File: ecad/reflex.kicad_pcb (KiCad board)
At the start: 2 copper layers, 20 x 60 mm, 29 parts, among them J1 USB_MICRO_B_SMD_2, J2 CONN_02X04_RA, Q1 BPW85C, SW1 CHERRY_MX1A-E1NW_BLUE, SW2 B3U-3000P_SPST-NO_SMD, U1 USBLC6, U2 ATSAMD21E18A, U3 AP2112K-3.3, U4 APA102-2020, X1 SWD_SMT_SOCKET

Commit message: Continued placement concepts and packaging ideas
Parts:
- removed D4: LED_YELLOW_1608M, Applidyne_LED:LEDC1608X80L40N
- removed D5: LED_GREEN_1608M, Applidyne_LED:LEDC1608X80L40N
- removed D7: BAV99, Applidyne_SOT:SOT95P240X110-3L16N
- removed R5, R6: 1K50_1608M, Applidyne_Resistor:RESC1608X50N
- added D3: BAV99_DUAL, Applidyne_SOT:SOT-363-6N, F.Cu at (99.5, 105.5)
- added U5: APA102-2020, Applidyne_LED:AP102_200X200X90L, F.Cu at (93.5, 116.5)
- moved C3 17.4 mm to (86.4, 93.7), turned to 270 degrees
- moved R4 15.1 mm to (82.1, 97.1)
- moved U4 14.2 mm to (93.5, 98.8), turned to 270 degrees
- moved R9 13.1 mm to (100.0, 118.5), turned to 180 degrees
- moved C2 12.7 mm to (107.2, 99.3), turned to 270 degrees
- moved R7 11.6 mm to (102.4, 104.9), turned to 270 degrees
- moved D1 3.22 mm to (96.5, 105.5)
- moved D2 3.22 mm to (93.5, 105.5)
- moved Q1 2.80 mm to (100.0, 77.8)
- moved R8 2.58 mm to (94.1, 110.2), turned to 90 degrees
- moved C1 2.40 mm to (105.0, 77.2)
- moved R2 2.40 mm to (105.1, 78.9)
- moved SW1 2.40 mm to (102.5, 82.3)
- moved U2 1.88 mm to (101.4, 98.2), turned to 0 degrees
- moved J2 0.75 mm to (97.5, 109.0)
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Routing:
- net Net-(U4-Pad1): track 0.00 -> 18.2 mm
- net Net-(U4-Pad6): track 0.00 -> 17.9 mm
- net EXTERNAL_TRIG: track 3.55 -> 17.3 mm
- net Net-(J2-Pad5): track 11.4 -> 2.18 mm
- net STATUS_CAPTURE: track 14.4 -> 6.23 mm
- net Net-(R4-Pad1): track 5.53 -> 0.00 mm
- net STATUS_USER: track 5.47 -> 0.00 mm
- net STATUS_TRIGGER: track 12.6 -> 7.37 mm
- net Net-(D5-PadA): track 4.10 -> 0.00 mm
- net Net-(J2-Pad4): track 4.27 -> 7.66 mm
- net Net-(D4-PadA): track 2.75 -> 0.00 mm
- net Net-(J2-Pad3): track 3.04 -> 5.74 mm
- net GND: track 8.90 -> 6.36 mm, vias 7 -> 4
- net UART_RX: track 8.65 -> 6.34 mm
- net UART_TX: track 8.03 -> 6.21 mm
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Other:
- board size 20 x 60 mm -> 20 x 58 mm

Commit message: Routing completed
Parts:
- F1: value 0.5A_1210L_PTC -> F1
- moved R4 25.4 mm to (107.5, 96.4), turned to 270 degrees
- moved C3 8.88 mm to (95.0, 95.9), turned to 0 degrees
- moved X1 7.47 mm to (101.7, 99.7), turned to 180 degrees
- moved R7 0.80 mm to (103.2, 104.7), turned to 0 degrees
- moved C2 0.50 mm to (107.5, 99.7)
- moved F1 0.20 mm to (99.2, 127.0)
- moved U4 0.20 mm to (93.5, 99.0)
- turned D2 to 270 degrees
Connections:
- D2 pad 3: STATUS_TRIGGER -> STATUS_CAPTURE
- D2 pad 6: STATUS_CAPTURE -> STATUS_TRIGGER
- SW2 pad 1: ~RESET -> GND
- SW2 pad 2: GND -> ~RESET
- X1 pad 7: Net-(X1-Pad7) -> PHOTO_TRANS
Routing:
- net Net-(Q1-PadC): track 0.00 -> 52.8 mm
- net +3.3V: track 6.33 -> 53.1 mm, vias 2 -> 8
- net USB_D-: track 0.00 -> 43.7 mm
- net USB_D+: track 0.00 -> 41.5 mm
- net PHOTO_TRANS: track 0.00 -> 31.2 mm, vias 0 -> 4
- net GND: track 6.36 -> 31.2 mm, vias 4 -> 14
- net ~RESET: track 0.00 -> 24.2 mm, vias 0 -> 2
- net STATUS_CAPTURE: track 6.23 -> 22.7 mm, vias 0 -> 1
- net LED_CLK: track 0.00 -> 16.1 mm, vias 0 -> 2
- net STATUS_TRIGGER: track 7.37 -> 21.9 mm, vias 0 -> 1
- net +5V: track 11.5 -> 23.8 mm
- net SWITCH_TRIG: track 11.8 -> 22.9 mm
- net LED_DATA: track 0.00 -> 10.7 mm, vias 0 -> 2
- net Net-(R4-Pad1): track 0.00 -> 10.1 mm
- net EXTERNAL_TRIG: track 17.3 -> 27.4 mm, vias 0 -> 2
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- added copper zone on B.Cu, net +3.3V
- added copper zone on B.Cu, net GND
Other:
- board size 20 x 58 mm -> 20 x 55 mm
- board text added: "1.0"

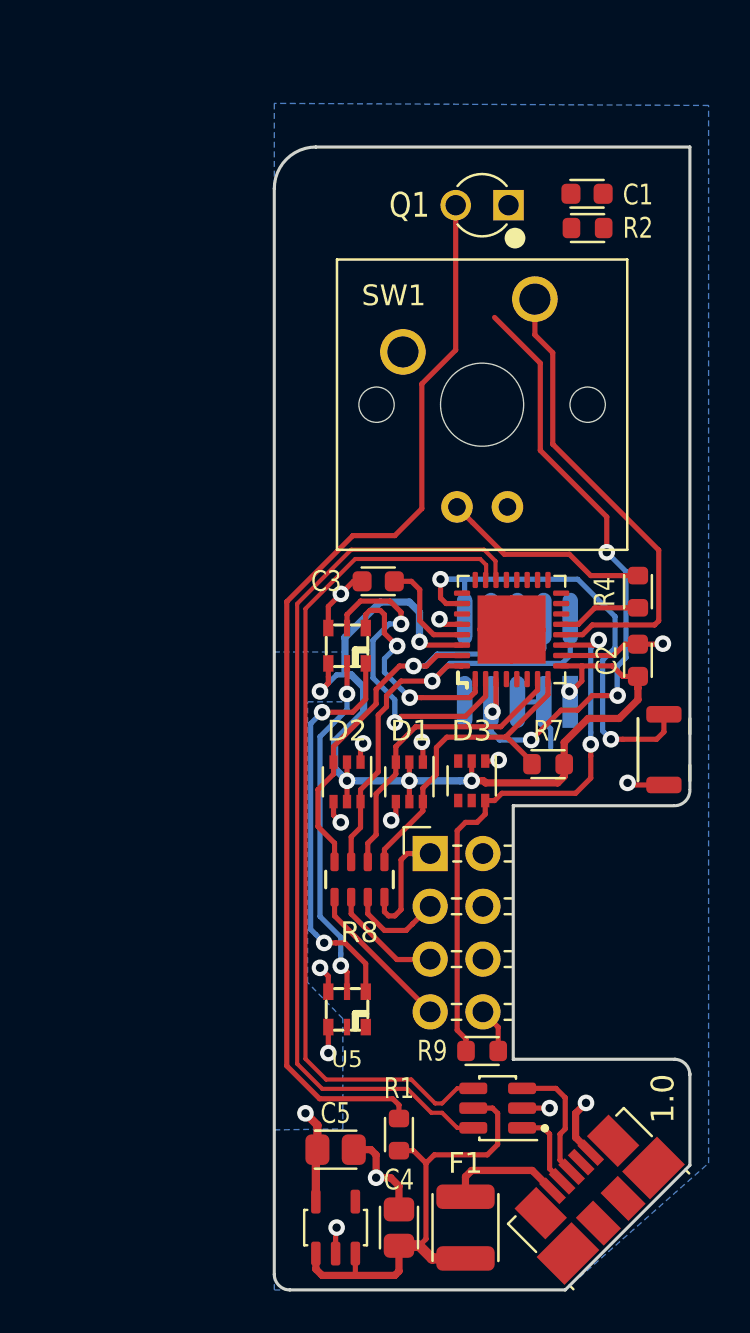
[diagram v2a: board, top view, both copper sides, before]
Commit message: Board outline cleanup, cosmetics
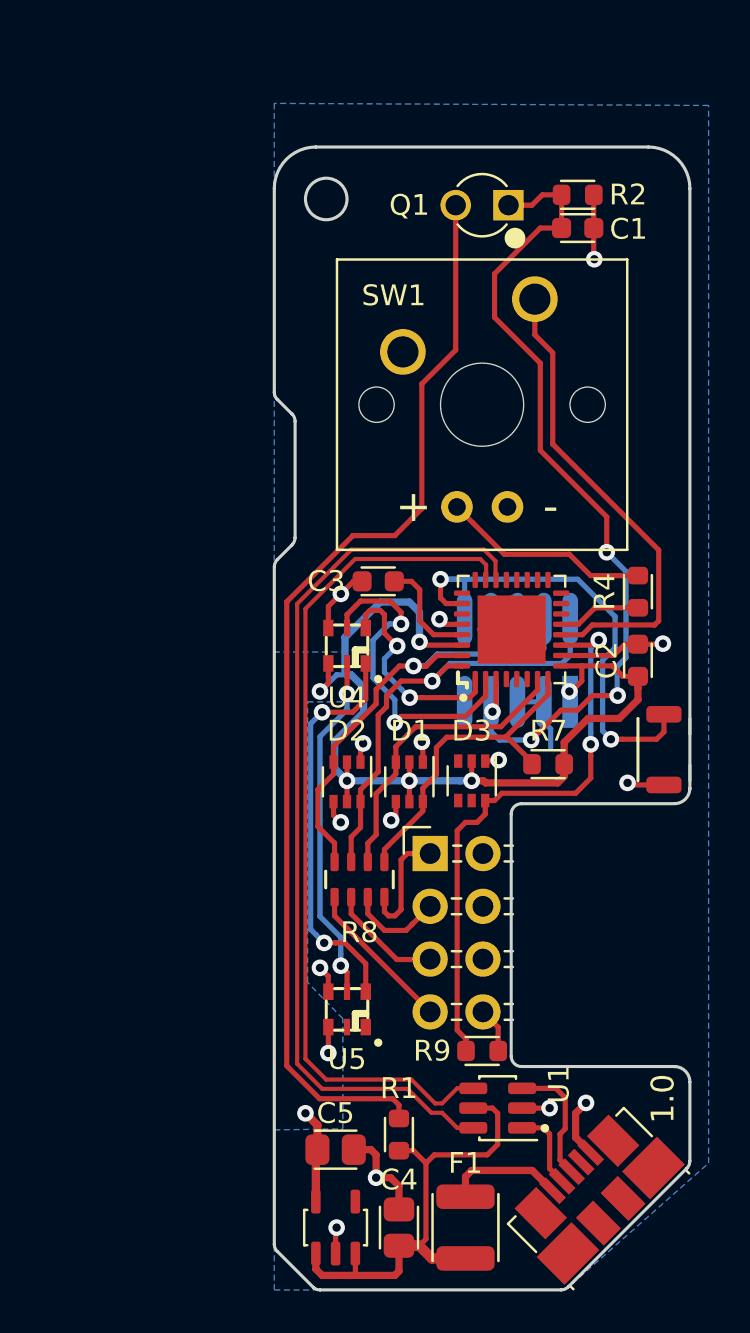
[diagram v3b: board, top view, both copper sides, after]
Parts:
- moved C1 1.71 mm to (104.6, 78.9)
- moved R2 1.67 mm to (104.6, 77.3)
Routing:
- net PHOTO_TRANS: track 31.2 -> 41.8 mm
- net GND: track 31.2 -> 34.3 mm, vias 14 -> 15
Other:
- outline, holes or cut-outs redrawn
- board text added: "+"
- board text added: "-"
- board text added: "KEYCAP"
- board text added: "S.RAPSON 2019"

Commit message: Comments on PCB file
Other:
- board text added: "Board Stackup 55x20 mm 1.6mm or 2.0mm thick FR4 2 layer, 35um (1 oz) copper ENIG or HASL finish OK"
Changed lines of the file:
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@@
   (general
     (thickness 2)
-    (drawings 53)
+    (drawings 54)
     (tracks 422)
     (zones 0)
@@
     )
   )
+  (gr_text "Board Stackup\n\n55x20 mm\n1.6mm or 2.0mm thick FR4\n2 layer, 35um (1 oz) copper\nENIG or HASL finish OK\n" (at 135.8 96) (layer Cmts.User)
+    (effects (font (size 3 3) (thickness 0.3)) (justify left))
+  )
   (gr_text "S.RAPSON 2019" (at 108 85.15 90) (layer B.SilkS)
